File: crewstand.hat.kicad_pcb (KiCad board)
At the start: 2 copper layers, 90 x 75 mm, 22 parts, among them J1 GPIO, J2 CAN Terminal, J3 Sensor Terminal, J4 V-In, J6 V-Out, J7 Relais2, J8 Relais1, U2 MCP2515-xSO, U3 MCP2551-I-P, U4 PicoW, Y2 12M

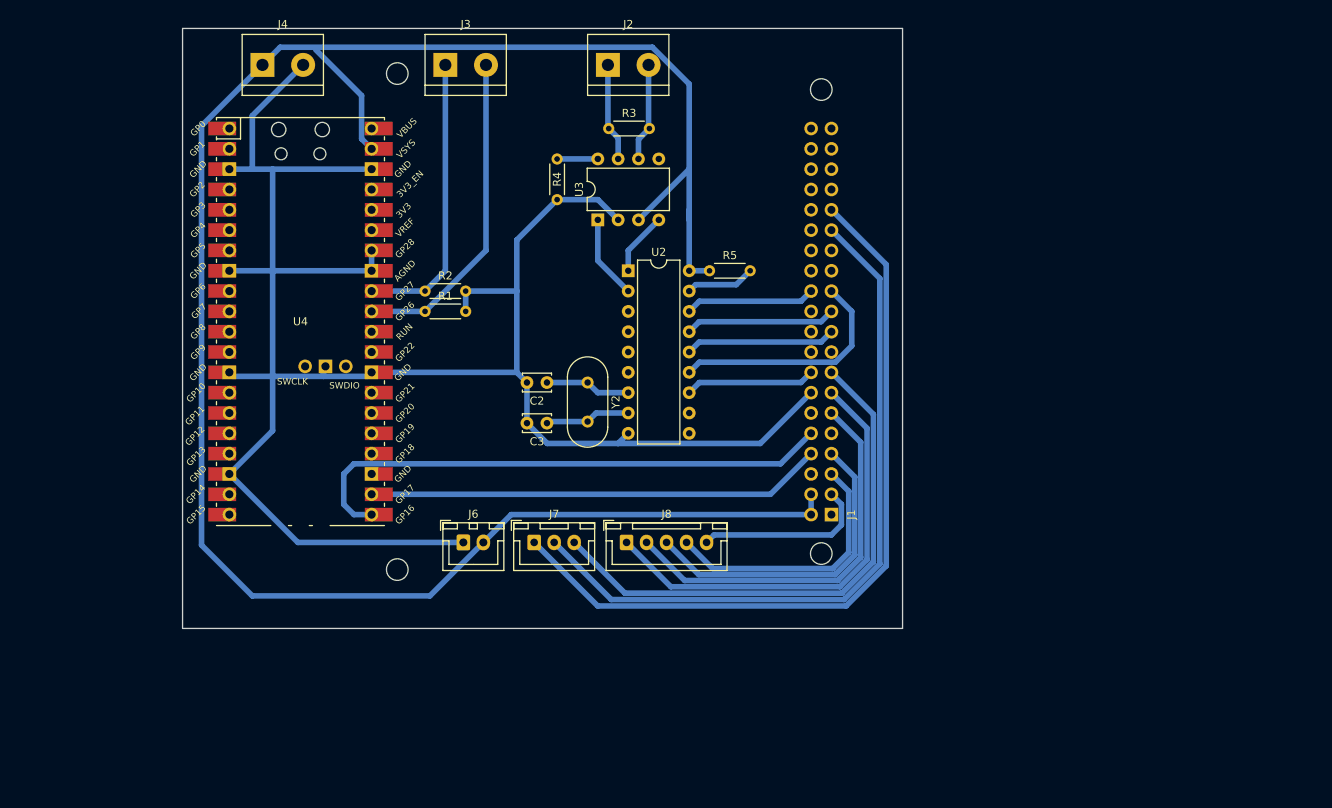
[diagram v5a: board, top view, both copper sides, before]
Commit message: feat: switch to professional PCB manufacturing service
- Update design rules for professional PCB manufacturing
- Prepare files for PCBWay or similar manufacturer submission
- use two layers for routing
    - use GND / 5V fill on layers
-  place silkscreen notes
- add redundant screw terminal for relais board connection

Resolves: #7
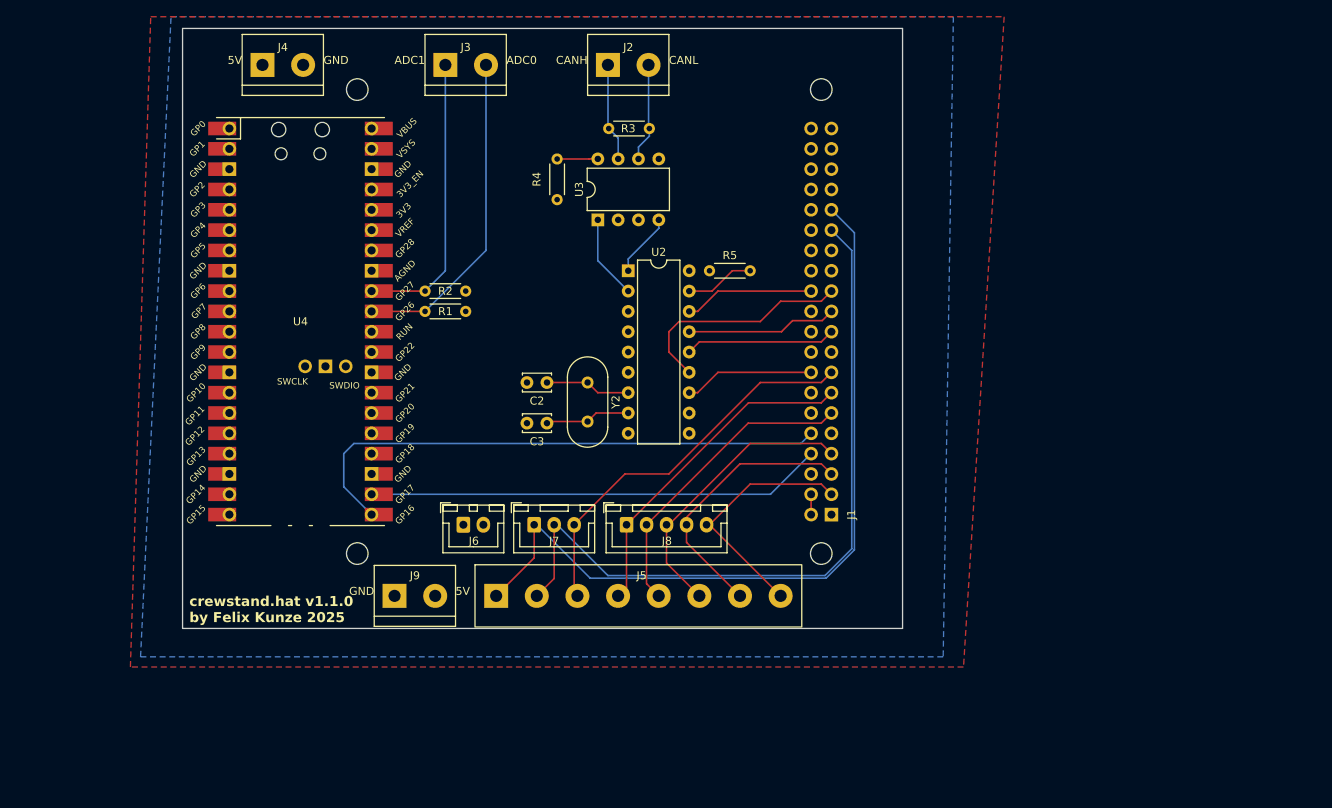
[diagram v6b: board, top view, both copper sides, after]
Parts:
- removed ? (x2): , 
- added J5: Screw_Terminal_01x08, TerminalBlock:TerminalBlock_bornier-8_P5.08mm, F.Cu at (201.9, 185.4)
- added J9: V-Out, TerminalBlock:TerminalBlock_bornier-2_P5.08mm, F.Cu at (189.2, 185.4)
- added REF**: MountingHole_2.7mm_M2.5, MountingHole:MountingHole_2.7mm_M2.5, F.Cu at (184.6, 180.1)
- added REF4: MountingHole_2.7mm_M2.5, MountingHole:MountingHole_2.7mm_M2.5, F.Cu at (184.6, 122.1)
- moved J6 2.21 mm to (197.8, 176.5)
- moved J7 2.21 mm to (206.7, 176.5)
- moved J8 2.21 mm to (218.2, 176.5)
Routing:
- net +5V: track 256.3 -> 2.54 mm
- net GND: track 253.8 -> 0.00 mm
- net /GPIO22: track 67.5 -> 49.1 mm
- net /GPIO27: track 56.5 -> 41.8 mm
- net /GPIO17: track 49.5 -> 38.4 mm
- net /GPIO2/SDA1: track 22.1 -> 30.8 mm
- net /GPIO4/GPCLK0: track 40.1 -> 35.9 mm
- net /GPIO5: track 89.7 -> 91.9 mm
- net /GPIO6: track 96.7 -> 98.8 mm
- net /GPIO11/SPI0.SCLK: track 29.6 -> 28.6 mm
- added copper zone on F.Cu, net +5V
- added copper zone on B.Cu, net GND
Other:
- board text added: "5V"
- board text added: "ADC0"
- board text added: "ADC1"
- board text added: "CANH"
- board text added: "CANL"
- board text added: "GND"
- board text added: "crewstand.hat v1.1.0 by Felix Kunze 2025"

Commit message: fix(relais-gpio): use GPIO26 & 19
- GPIO 2&3 where high on boot
- ensures all pins are low until actively switched by backend
- minor changes on routing and footprints

issue #13
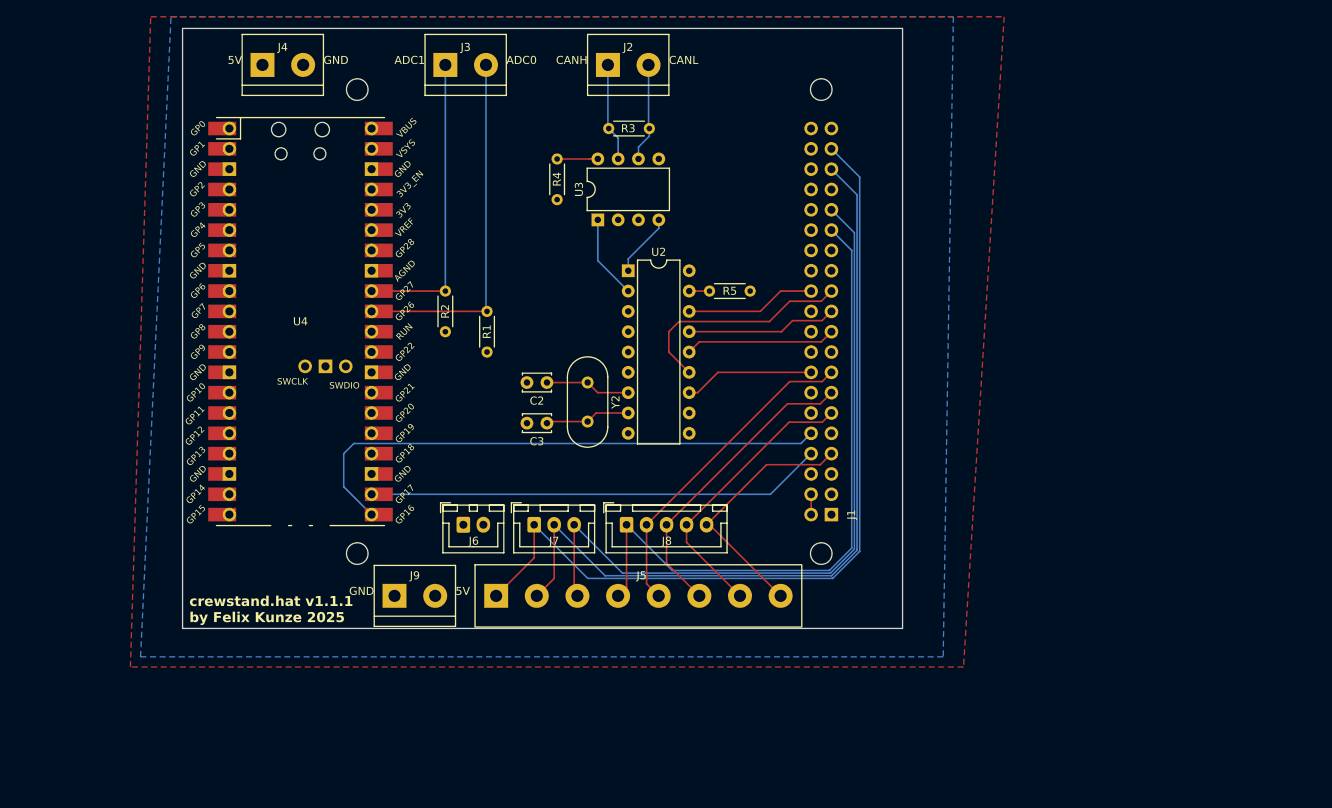
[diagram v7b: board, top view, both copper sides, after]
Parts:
- moved R1 7.75 mm to (200.8, 149.9), turned to -90 degrees
- moved R5 5.68 mm to (233.7, 147.3), turned to 180 degrees
- moved R2 2.54 mm to (195.6, 147.3), turned to -90 degrees
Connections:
- J5 pad 1: /GPIO6 -> /GPIO26
- J5 pad 2: /GPIO5 -> /GPIO19/PCM.FS
- J5 pad 3: /GPIO22 -> /GPIO6
- J5 pad 4: /GPIO27 -> /GPIO5
- J5 pad 5: /GPIO17 -> /GPIO22
- J5 pad 6: /GPIO4/GPCLK0 -> /GPIO27
- J5 pad 7: /GPIO3/SCL1 -> /GPIO17
- J5 pad 8: /GPIO2/SDA1 -> /GPIO4/GPCLK0
- J7 pad 1: /GPIO6 -> /GPIO26
- J7 pad 2: /GPIO5 -> /GPIO19/PCM.FS
- J7 pad 3: /GPIO22 -> /GPIO6
- J8 pad 1: /GPIO27 -> /GPIO5
- J8 pad 2: /GPIO17 -> /GPIO22
- J8 pad 3: /GPIO4/GPCLK0 -> /GPIO27
- J8 pad 4: /GPIO3/SCL1 -> /GPIO17
- J8 pad 5: /GPIO2/SDA1 -> /GPIO4/GPCLK0
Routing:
- net /GPIO26: track 0.00 -> 107.5 mm
- net /GPIO19/PCM.FS: track 0.00 -> 100.6 mm
- net /GPIO3/SCL1: track 33.1 -> 0.00 mm
- net /GPIO2/SDA1: track 30.8 -> 0.00 mm
- net /GPIO5: track 91.9 -> 81.8 mm
- net /GPIO22: track 49.1 -> 40.5 mm
- net /GPIO6: track 98.8 -> 91.4 mm
- net Net-(U2-~{RESET}): track 8.67 -> 2.54 mm
- net Net-(J3-Pin_2): track 40.6 -> 45.2 mm
- net /GPIO27: track 41.8 -> 38.0 mm
- net /GPIO4/GPCLK0: track 35.9 -> 32.2 mm
- net /GPIO17: track 38.4 -> 35.6 mm
- net Net-(J3-Pin_1): track 36.0 -> 37.5 mm
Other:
- board text added: "crewstand.hat v1.1.1 by Felix Kunze 2025"
- board text removed: "crewstand.hat v1.1.0 by Felix Kunze 2025"
